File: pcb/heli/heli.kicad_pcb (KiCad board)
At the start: 4 copper layers, 50.6 x 50 mm, 75 parts, among them J1 Batterie, J2 Debug, J3 CONMHF4-SMD-G-T, J4 Servo, J5 Servo, M1 Motor_DC, M2 Motor_DC, Q1 IRLZ44N, Q2 BC547, Q3 IRLZ44N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

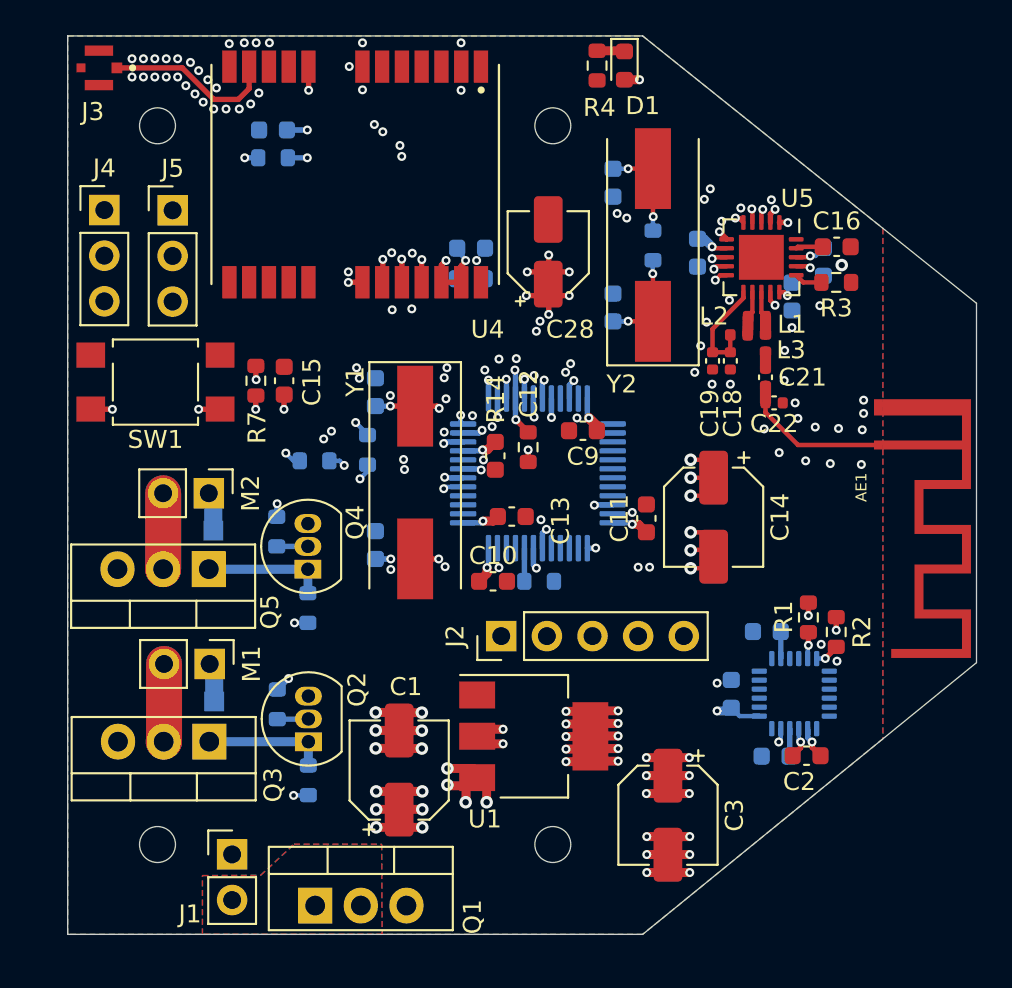
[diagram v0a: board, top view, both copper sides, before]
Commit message: 
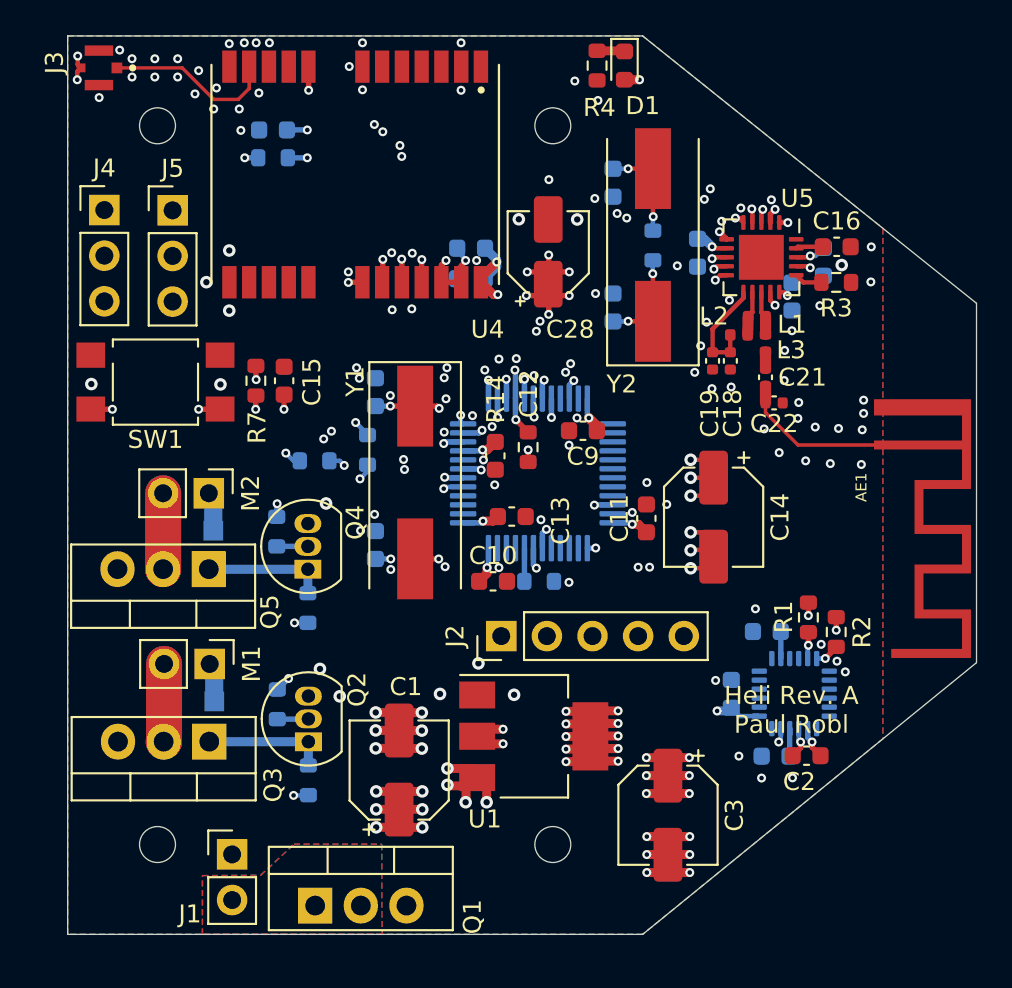
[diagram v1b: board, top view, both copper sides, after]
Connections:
- net /Radio/50ohm renamed /Radio/RADIO50ohm
- net Net-(J3-Pad1) renamed /GPS/GPS50ohms
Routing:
- net GND: track 20.9 -> 27.1 mm, vias 113 -> 143
- net 7.4V: track 16.7 -> 16.0 mm
- net 3.3V: track 59.7 -> 59.1 mm
- added copper zone on In1.Cu, net GND
- added copper zone on In2.Cu, net GND
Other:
- board text added: "Heli Rev. A Paul Robl"

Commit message: Removed MPU6050, updated pcb
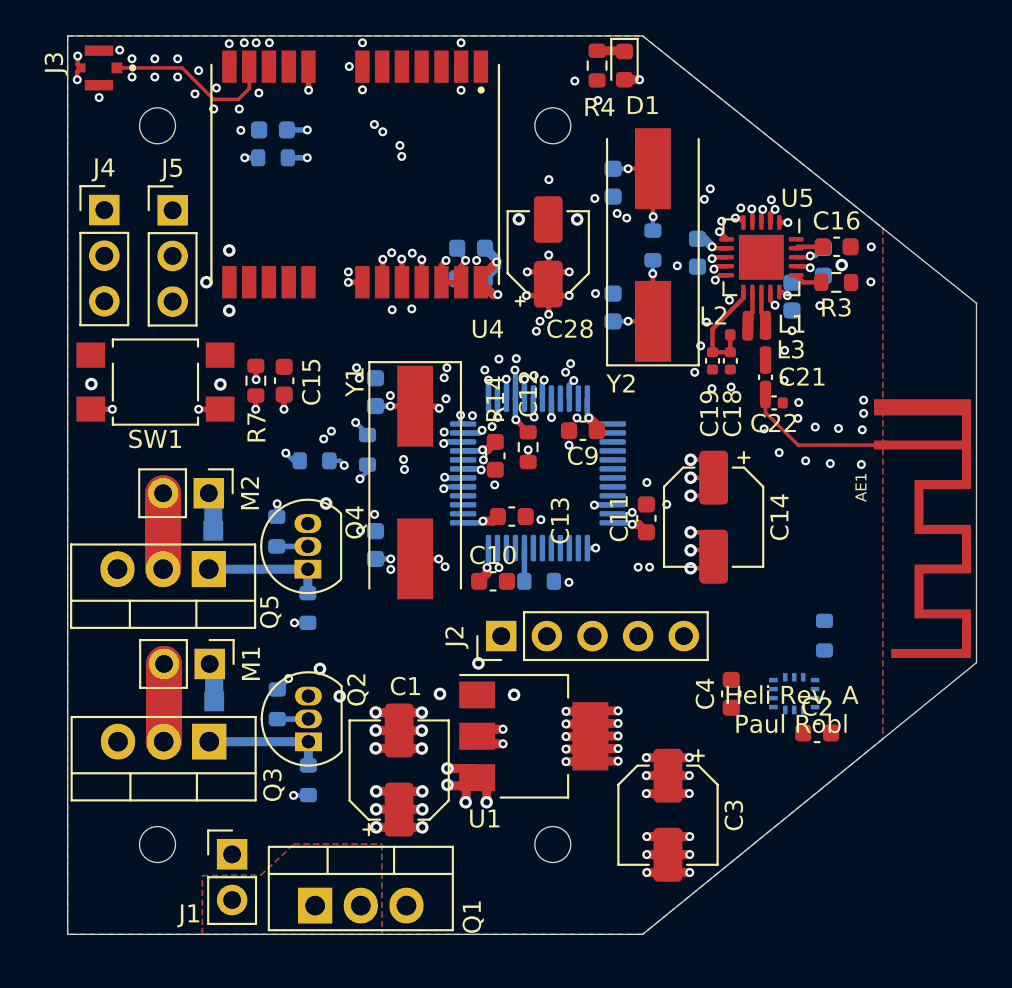
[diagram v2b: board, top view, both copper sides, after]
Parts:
- removed C5: 100nF, Capacitor_SMD:C_0603_1608Metric
- removed C8: 2.2nF 50V, Capacitor_SMD:C_0603_1608Metric
- removed R1, R2: 10k, Resistor_SMD:R_0603_1608Metric
- added R16: 1M, Resistor_SMD:R_0603_1608Metric, B.Cu at (60.1, 48.4)
- C2: value 10nF -> 100nF
- C4: moved to F.Cu
- U2: value MPU-6050 -> BMI270; footprint Sensor_Motion:InvenSense_QFN-24_4x4mm_P0.5mm -> lib:XDCR_BMI270
- moved C2 1.39 mm to (59.7, 53.8), turned to 0 degrees
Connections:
- U2 pad 1: GND -> SPI2_MISO
- U2 pad 10: Net-(C5-Pad1) -> unconnected-(U2-Pad10)
- U2 pad 11: GND -> unconnected-(U2-Pad11)
- U2 pad 12: unconnected-(U2-Pad12) -> IMU_CSN
- U2 pad 13: 3.3V -> SPI2_SCK
- U2 pad 14: unconnected-(U2-Pad14) -> SPI2_MOSI
- U2 pad 5: unconnected-(U2-Pad5) -> 3.3V
- U2 pad 6: unconnected-(U2-Pad6) -> GND
- U2 pad 7: unconnected-(U2-Pad7) -> GND
- U2 pad 9: GND -> unconnected-(U2-Pad9)
- U3 pad 25: unconnected-(U3-Pad25) -> IMU_CSN
- U3 pad 26: unconnected-(U3-Pad26) -> SPI2_SCK
- U3 pad 27: unconnected-(U3-Pad27) -> SPI2_MISO
- U3 pad 28: unconnected-(U3-Pad28) -> SPI2_MOSI
- U3 pad 42: I2C_SCL -> unconnected-(U3-Pad42)
- U3 pad 43: I2C_SDA -> unconnected-(U3-Pad43)
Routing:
- net I2C_SDA: track 20.7 -> 0.00 mm, vias 2 -> 0
- net I2C_SCL: track 20.2 -> 0.00 mm, vias 2 -> 0
- net 3.3V: track 59.1 -> 53.5 mm, vias 47 -> 43
- net GND: track 27.1 -> 24.3 mm, vias 143 -> 133
- net Net-(C5-Pad1): track 1.51 -> 0.00 mm
- net Net-(C8-Pad1): track 1.50 -> 0.00 mm

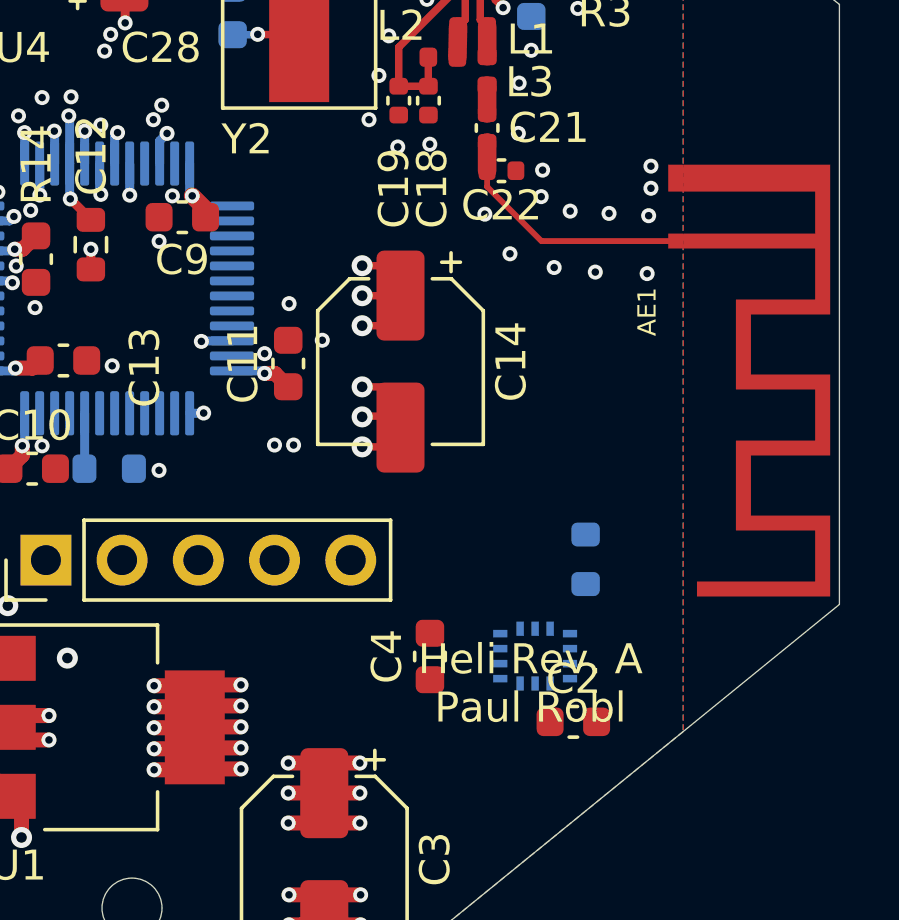
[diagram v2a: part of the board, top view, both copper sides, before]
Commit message: Added BMM150 as BMI270 i2c slave
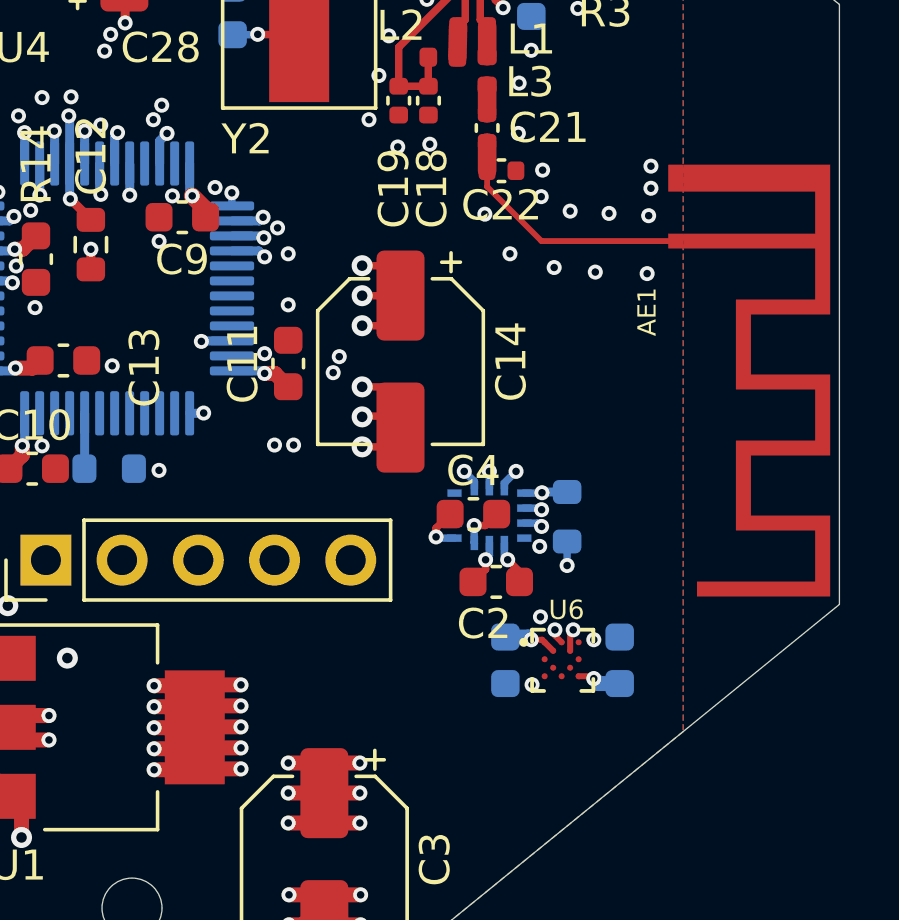
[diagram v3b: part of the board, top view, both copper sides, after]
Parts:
- added C5: 100nF, Capacitor_SMD:C_0603_1608Metric, B.Cu at (61.3, 51.7)
- added C8: 100nF, Capacitor_SMD:C_0603_1608Metric, B.Cu at (57.4, 51.7)
- added U6: BMM150, lib:XDCR_BMM150, F.Cu at (59.4, 51.7)
- moved C2 5.33 mm to (57.1, 49.1), turned to 180 degrees
- moved C4 4.96 mm to (56.4, 46.9), turned to 0 degrees
- moved U2 4.93 mm to (56.9, 46.9)
- moved R16 1.55 mm to (59.5, 47.0), turned to 90 degrees
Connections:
- U2 pad 2: unconnected-(U2-Pad2) -> /IMU/SDA
- U2 pad 3: unconnected-(U2-Pad3) -> /IMU/SCL
- U2 pad 4: unconnected-(U2-Pad4) -> /IMU/INT1
- U2 pad 9: unconnected-(U2-Pad9) -> /IMU/INT2
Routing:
- net SPI2_MISO: track 0.00 -> 19.3 mm, vias 0 -> 2
- net SPI2_MOSI: track 0.00 -> 16.4 mm, vias 0 -> 2
- net IMU_CSN: track 0.00 -> 15.2 mm, vias 0 -> 2
- net SPI2_SCK: track 0.00 -> 14.4 mm, vias 0 -> 3
- net /IMU/SDA: track 0.00 -> 7.13 mm, vias 0 -> 2
- net 3.3V: track 53.5 -> 60.3 mm, vias 43 -> 48
- net /IMU/SCL: track 0.00 -> 4.76 mm, vias 0 -> 2
- net GND: track 24.3 -> 27.3 mm, vias 133 -> 142

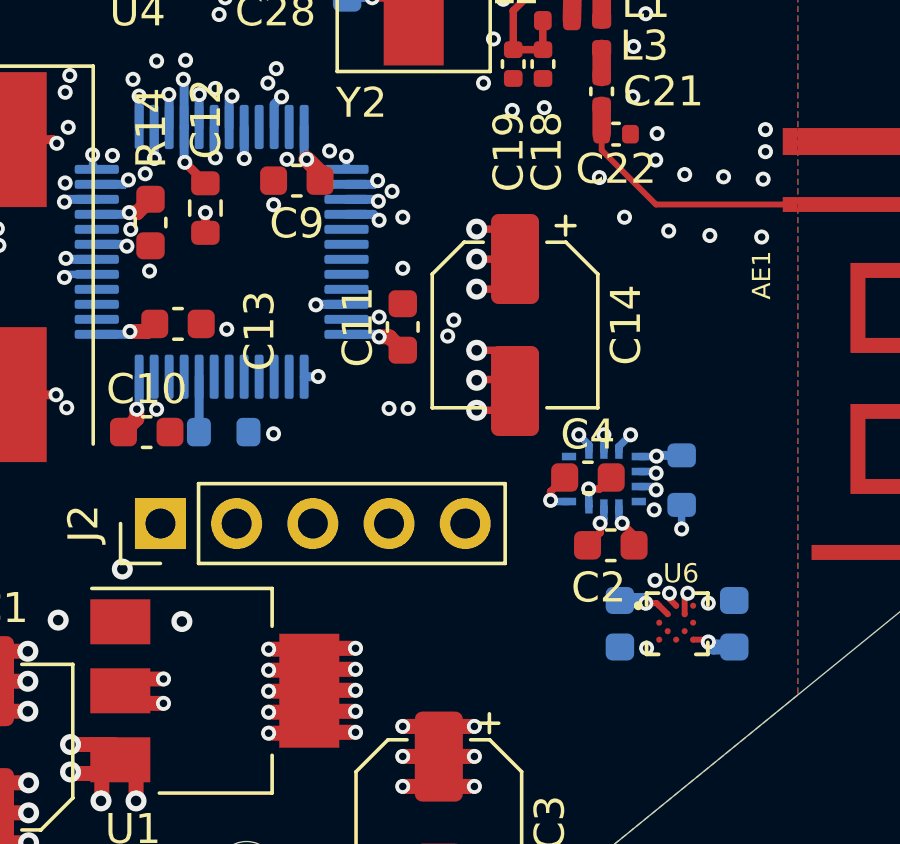
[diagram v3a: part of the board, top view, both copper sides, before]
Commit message: 
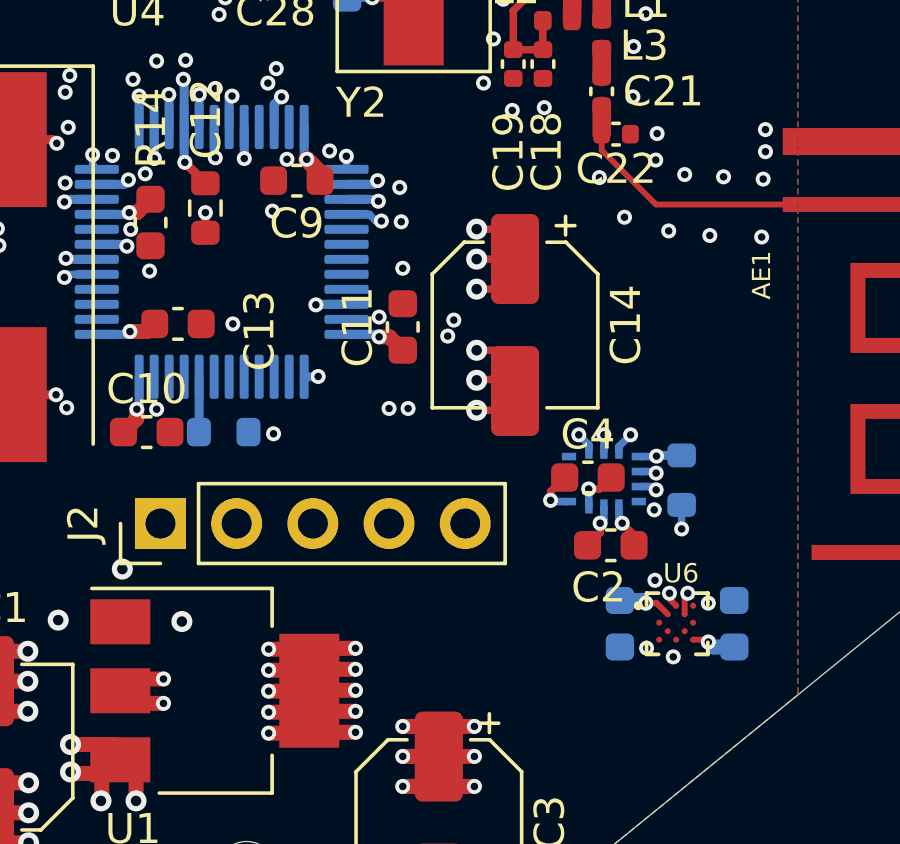
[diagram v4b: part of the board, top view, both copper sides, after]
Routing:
- net IMU_CSN: track 15.2 -> 16.4 mm
- net SPI2_SCK: track 14.4 -> 15.4 mm
- net GND: vias 142 -> 143

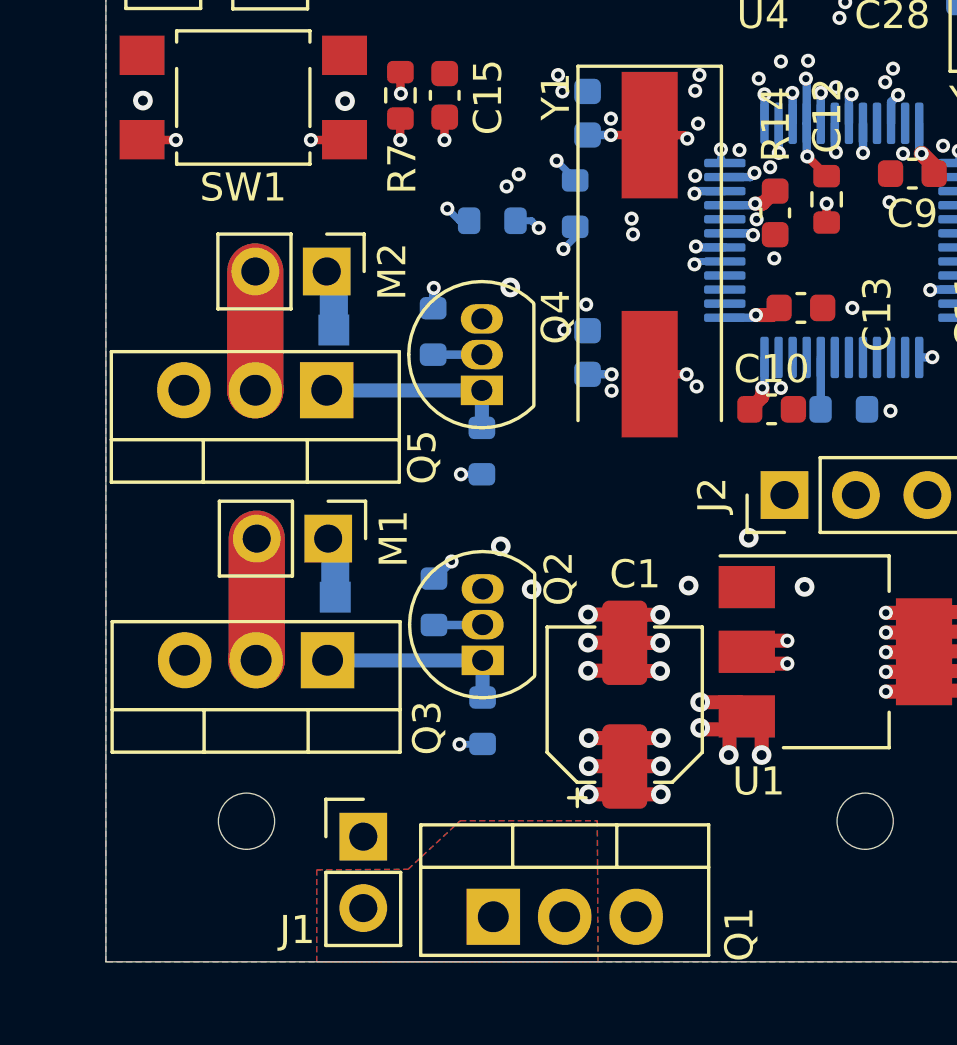
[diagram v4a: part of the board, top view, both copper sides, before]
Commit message: 
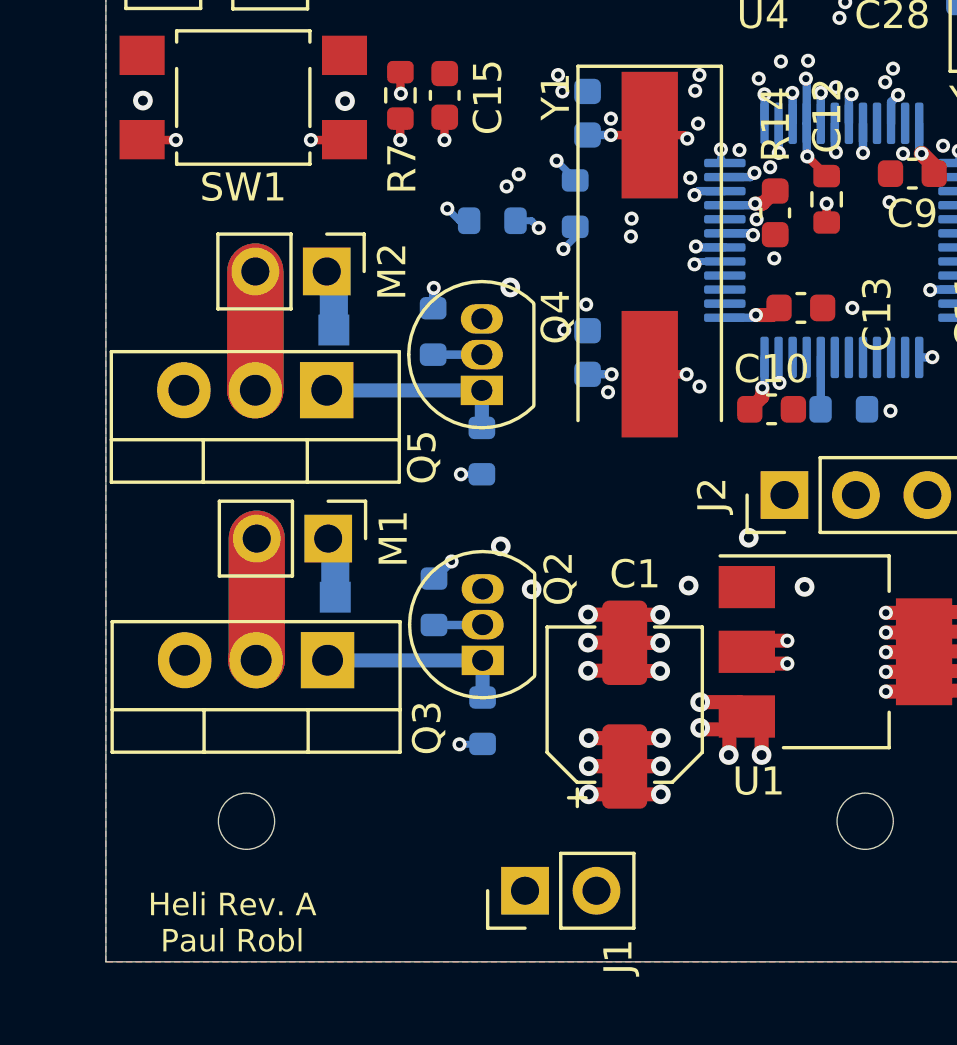
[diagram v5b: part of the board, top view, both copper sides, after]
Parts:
- removed Q1: IRLZ44N, Package_TO_SOT_THT:TO-220-3_Vertical
- moved J1 6.07 mm to (32.9, 62.5), turned to 90 degrees
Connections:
- J1 pad 2: /Batt- -> GND
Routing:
- removed copper zone on B.Cu, net /Batt-
- removed copper zone on F.Cu, net /Batt-
